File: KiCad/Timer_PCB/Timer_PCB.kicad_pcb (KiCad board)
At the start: 2 copper layers, 102 x 75.5 mm, 2 parts

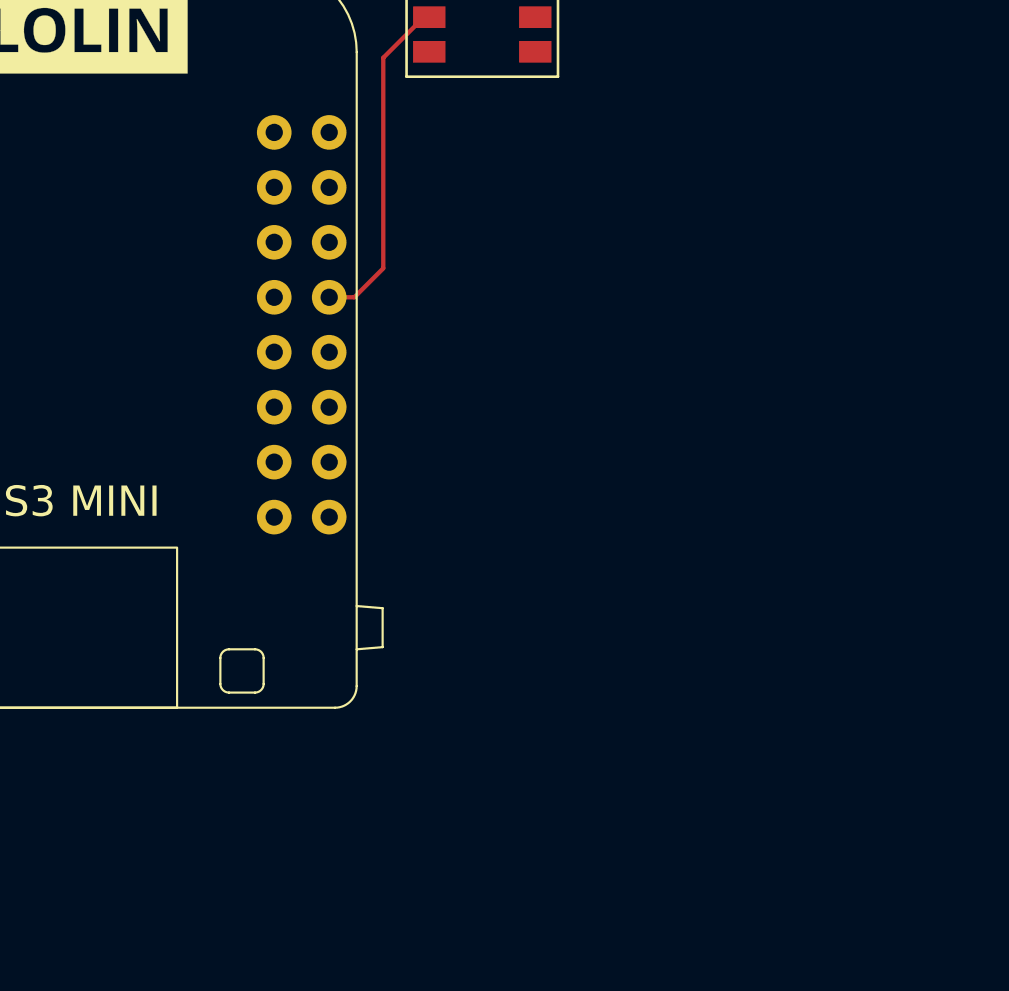
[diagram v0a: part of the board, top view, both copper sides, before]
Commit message: Ajout de la différenciation SMD et THT dans l'article composants electroniques. Ajout de la marche à suivre pour passer d'un composant physique à la réalisation de son schematic sur kicad. recherche de schéma du composant. recherche du numero de part sur JLC, recherche du package. modification du symbole pour y inclure ces information.
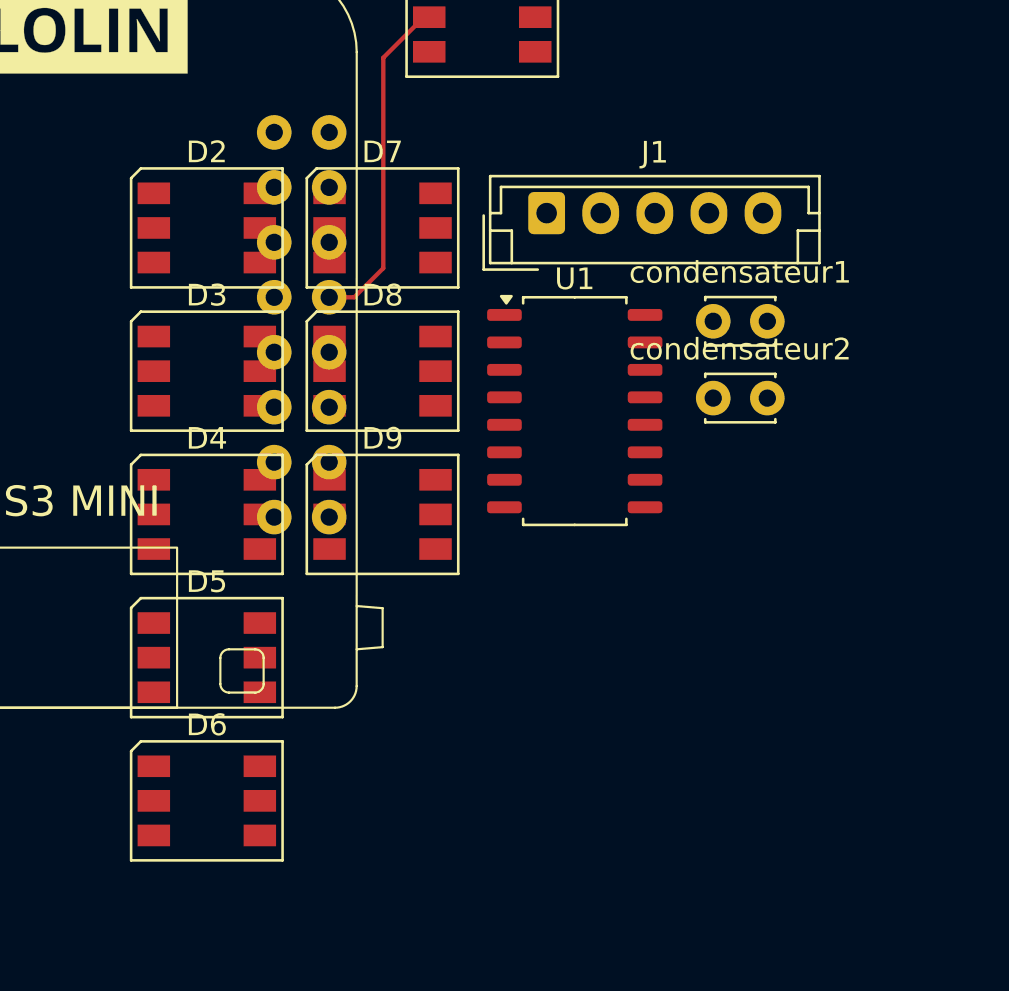
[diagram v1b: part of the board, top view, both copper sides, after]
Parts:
- added D2: WS2812, LED_SMD:LED_WS2812_PLCC6_5.0x5.0mm_P1.6mm, F.Cu at (101.3, 69.6)
- added D3: WS2812, LED_SMD:LED_WS2812_PLCC6_5.0x5.0mm_P1.6mm, F.Cu at (101.3, 76.3)
- added D4: WS2812, LED_SMD:LED_WS2812_PLCC6_5.0x5.0mm_P1.6mm, F.Cu at (101.3, 82.9)
- added D5: WS2812, LED_SMD:LED_WS2812_PLCC6_5.0x5.0mm_P1.6mm, F.Cu at (101.3, 89.5)
- added D6: WS2812, LED_SMD:LED_WS2812_PLCC6_5.0x5.0mm_P1.6mm, F.Cu at (101.3, 96.1)
- added D7: WS2812, LED_SMD:LED_WS2812_PLCC6_5.0x5.0mm_P1.6mm, F.Cu at (109.5, 69.6)
- added D8: WS2812, LED_SMD:LED_WS2812_PLCC6_5.0x5.0mm_P1.6mm, F.Cu at (109.5, 76.3)
- added D9: WS2812, LED_SMD:LED_WS2812_PLCC6_5.0x5.0mm_P1.6mm, F.Cu at (109.5, 82.9)
- added J1: JST_05, Connector_JST:JST_EH_B5B-EH-A_1x05_P2.50mm_Vertical, F.Cu at (117.0, 69.0)
- added U1: ULN2003, Package_SO:SOIC-16_4.55x10.3mm_P1.27mm, F.Cu at (118.3, 78.1)
- added condensateur1: 10uF, Capacitor_THT:C_Disc_D3.0mm_W2.0mm_P2.50mm, F.Cu at (124.8, 74.0)
- added condensateur2: 100nF, Capacitor_THT:C_Disc_D3.0mm_W2.0mm_P2.50mm, F.Cu at (124.8, 77.5)
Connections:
- D1 pad 1: unconnected-(D1-DOUT-Pad1) -> Net-(D1-DOUT)
- D1 pad 5: unconnected-(D1-VDD-Pad5) -> GND
- D1 pad 6: unconnected-(D1-VSS-Pad6) -> GND
- U2 pad 15: Net-(BT1-+) -> GND
- U2 pad 17: unconnected-(U2-GPIO33-Pad17) -> Net-(D1-DIN)
- U2 pad 2: unconnected-(U2-GPIO1-Pad2) -> M1A
- U2 pad 21: unconnected-(U2-GPIO38-Pad21) -> GND
- U2 pad 22: unconnected-(U2-GPIO36-Pad22) -> Net-(SW4-A)
- U2 pad 23: unconnected-(U2-GPIO34-Pad23) -> Net-(SW3-C)
- U2 pad 24: Net-(D1-DIN) -> Net-(SW3-A)
- U2 pad 25: unconnected-(U2-GPIO21-Pad25) -> GND
- U2 pad 26: unconnected-(U2-GPIO18-Pad26) -> GND
- U2 pad 27: unconnected-(U2-GPIO17-Pad27) -> GND
- U2 pad 28: unconnected-(U2-GPIO16-Pad28) -> Net-(SW1-A)
- U2 pad 29: Net-(BT1--) -> GND
- U2 pad 30: unconnected-(U2-GND-Pad30) -> GND
- U2 pad 5: unconnected-(U2-GPIO4-Pad5) -> M1B
- U2 pad 6: unconnected-(U2-GPIO5-Pad6) -> M1C
- U2 pad 7: unconnected-(U2-GPIO12-Pad7) -> M1D

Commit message: avancement de l'article sur l'utilisation de Kicad
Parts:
- added D10: WS2812, LED_SMD:LED_WS2812_PLCC6_5.0x5.0mm_P1.6mm, F.Cu at (105.2, 65.7)
- added D11: WS2812, LED_SMD:LED_WS2812_PLCC6_5.0x5.0mm_P1.6mm, F.Cu at (105.2, 72.3)
- added D12: WS2812, LED_SMD:LED_WS2812_PLCC6_5.0x5.0mm_P1.6mm, F.Cu at (105.2, 78.9)
- added D13: WS2812, LED_SMD:LED_WS2812_PLCC6_5.0x5.0mm_P1.6mm, F.Cu at (113.4, 65.7)
- added D14: WS2812, LED_SMD:LED_WS2812_PLCC6_5.0x5.0mm_P1.6mm, F.Cu at (113.4, 72.3)
- added D15: WS2812, LED_SMD:LED_WS2812_PLCC6_5.0x5.0mm_P1.6mm, F.Cu at (113.4, 78.9)
- added D16: WS2812, LED_SMD:LED_WS2812_PLCC6_5.0x5.0mm_P1.6mm, F.Cu at (121.5, 65.7)
- added D17: WS2812, LED_SMD:LED_WS2812_PLCC6_5.0x5.0mm_P1.6mm, F.Cu at (121.5, 72.3)
- added D18: WS2812, LED_SMD:LED_WS2812_PLCC6_5.0x5.0mm_P1.6mm, F.Cu at (121.5, 78.9)
- added J2: JST_05, Connector_JST:JST_EH_B5B-EH-A_1x05_P2.50mm_Vertical, F.Cu at (124.0, 84.8)
- added J3: JST_05, Connector_JST:JST_EH_B5B-EH-A_1x05_P2.50mm_Vertical, F.Cu at (124.0, 90.7)
- added U3: ULN2003, Package_SO:SOIC-16_4.55x10.3mm_P1.27mm, F.Cu at (106.0, 88.2)
- added U4: ULN2003, Package_SO:SOIC-16_4.55x10.3mm_P1.27mm, F.Cu at (115.7, 88.2)
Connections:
- net Net-(SW1-A) renamed Switch_Led_control_Down
- net Net-(SW3-A) renamed Switch_motor_2_Down
- net Net-(SW3-C) renamed Switch_motor_2_Up
- net Net-(SW4-A) renamed Switch_motor_3_Down
- U2 pad 10: unconnected-(U2-GPIO7-Pad10) -> M2C
- U2 pad 11: unconnected-(U2-GPIO11-Pad11) -> M2D
- U2 pad 12: unconnected-(U2-GPIO8-Pad12) -> M3A
- U2 pad 13: unconnected-(U2-GPIO10-Pad13) -> M3B
- U2 pad 14: unconnected-(U2-GPIO9-Pad14) -> M3C
- U2 pad 15: GND -> Net-(BT1-+)
- U2 pad 16: unconnected-(U2-GPIO14-Pad16) -> M3D
- U2 pad 17: Net-(D1-DIN) -> WS2812_Led
- U2 pad 21: GND -> Switch_motor_3_Up
- U2 pad 25: GND -> Switch_motor_1_Up
- U2 pad 26: GND -> Switch_motor_1_Down
- U2 pad 27: GND -> Switch_Led_control_Up
- U2 pad 29: GND -> unconnected-(U2-GND-Pad29)
- U2 pad 30: GND -> unconnected-(U2-GND-Pad30)
- U2 pad 31: unconnected-(U2-GPIO15-Pad31) -> Net-(U2-GPIO15)
- U2 pad 8: unconnected-(U2-GPIO6-Pad8) -> M2A
- U2 pad 9: unconnected-(U2-GPIO13-Pad9) -> M2B
- condensateur1 pad 1: GND -> Net-(U2-GPIO15)
- condensateur1 pad 2: GND -> Net-(BT1--)
- condensateur2 pad 1: GND -> Net-(U2-GPIO15)
- condensateur2 pad 2: GND -> Net-(BT1--)

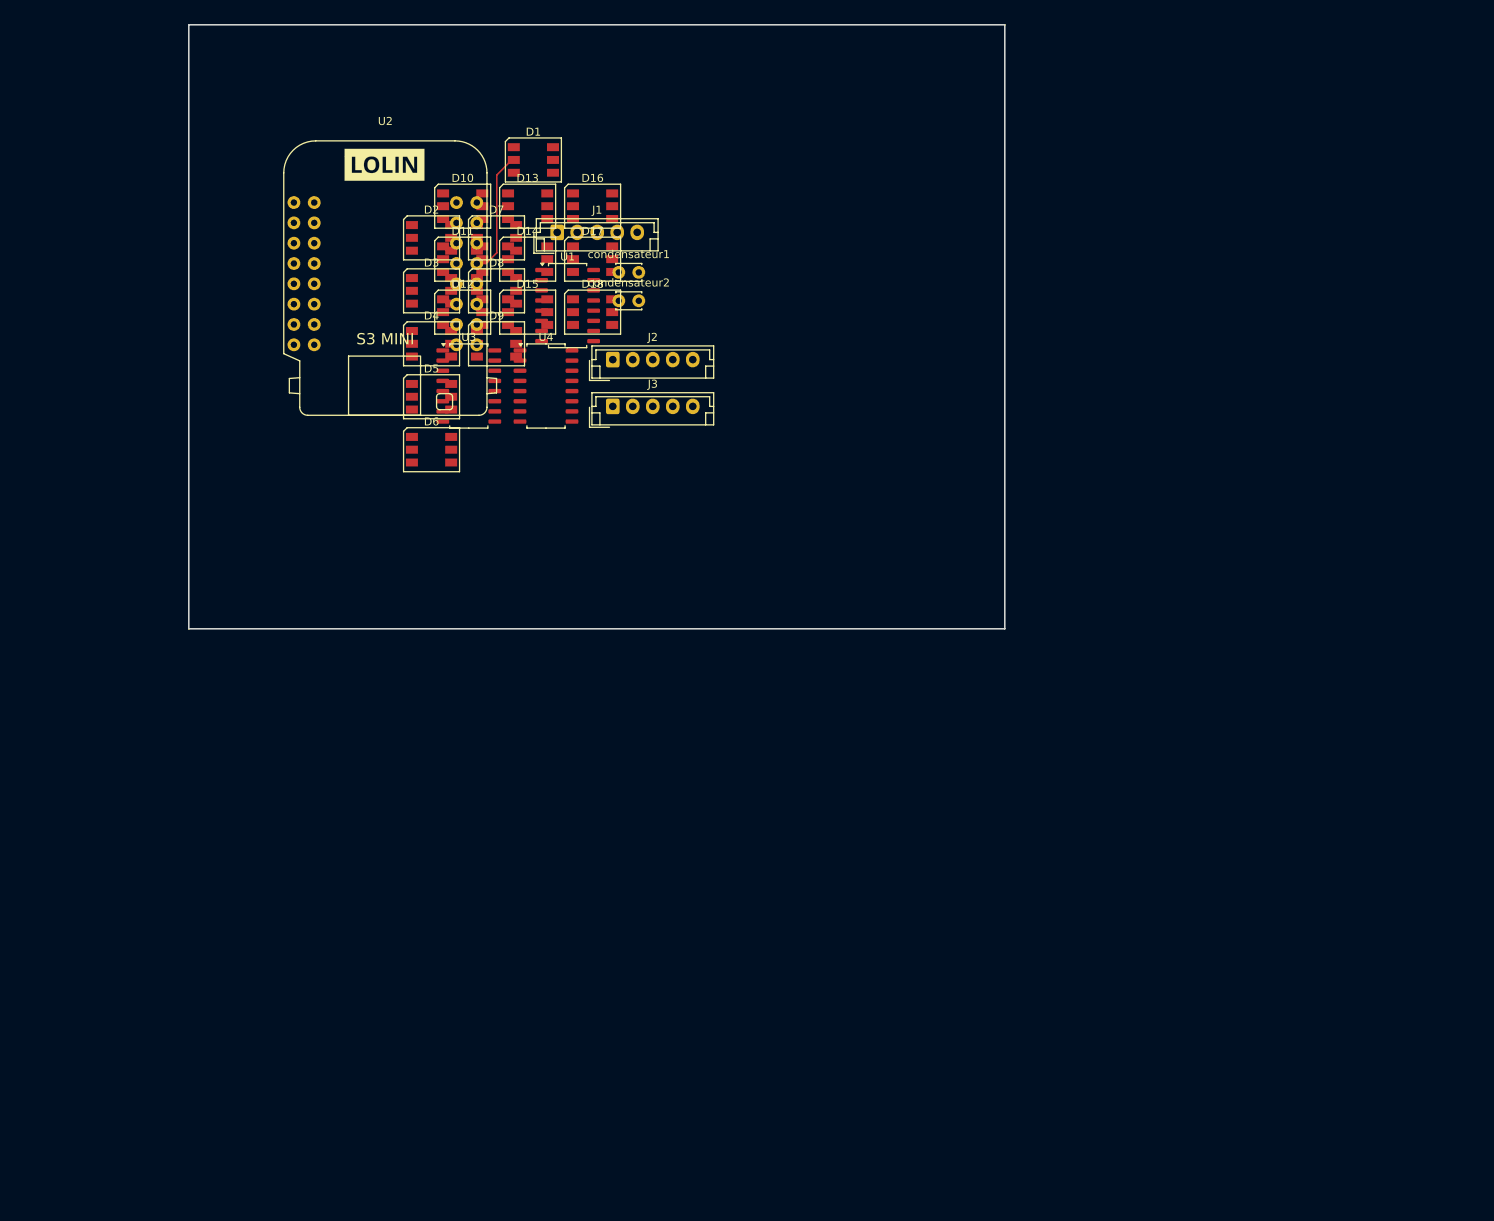
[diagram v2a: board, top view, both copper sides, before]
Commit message: dévellopement de l'article Kicad. Comment parametrer nbr couches PCB et créer zone connecté GND
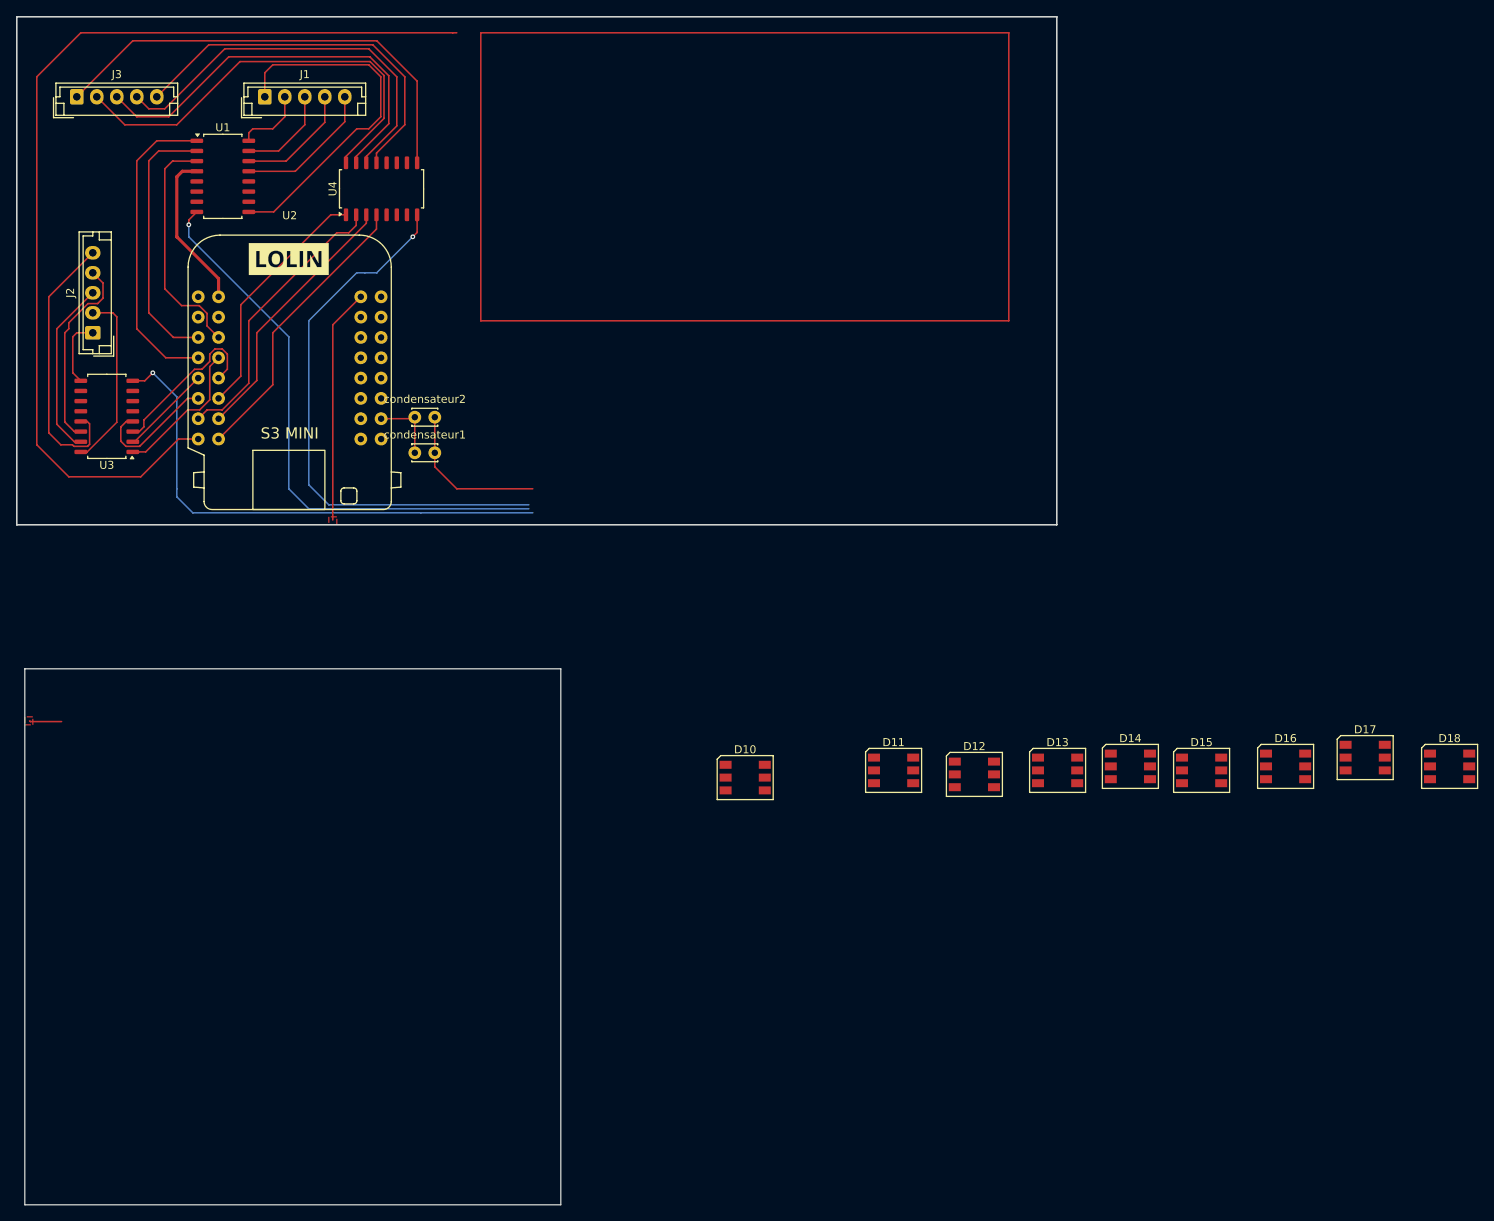
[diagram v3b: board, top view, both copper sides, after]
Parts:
- removed D1, D2, D3, D4, D5, D6, D7, D8, D9: WS2812, LED_SMD:LED_WS2812_PLCC6_5.0x5.0mm_P1.6mm
- moved D18 121.2 mm to (228.6, 135.7)
- moved D17 114.9 mm to (218.1, 134.6)
- moved D16 111.4 mm to (208.1, 135.7)
- moved D15 101.9 mm to (197.6, 136.2)
- moved D14 98.5 mm to (188.7, 135.7)
- moved D13 96.8 mm to (179.6, 136.2)
- moved D12 86.2 mm to (169.2, 136.7)
- moved D11 83.6 mm to (159.1, 136.2)
- moved D10 79.7 mm to (140.6, 137.1)
- moved J3 77.4 mm to (57.0, 52.0)
- moved J2 65.1 mm to (59.0, 81.5), turned to 90 degrees
- moved U1 46.0 mm to (75.2, 61.9)
- moved U3 45.4 mm to (60.8, 91.9), turned to 180 degrees
- moved J1 40.3 mm to (80.5, 52.0)
- moved condensateur1 34.0 mm to (99.2, 96.5)
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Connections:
- net WS2812_Led renamed WS2812_Med
- U2 pad 2: M1A -> M1D
- U2 pad 29: unconnected-(U2-GND-Pad29) -> GND
- U2 pad 30: unconnected-(U2-GND-Pad30) -> GND
- U2 pad 31: Net-(U2-GPIO15) -> unconnected-(U2-GPIO15-Pad31)
- U2 pad 7: M1D -> M1A
- condensateur1 pad 1: Net-(U2-GPIO15) -> GND
- condensateur2 pad 1: Net-(U2-GPIO15) -> GND
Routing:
- net GND: track 0.00 -> 214.3 mm, vias 0 -> 3
- net Net-(BT1-+): track 0.00 -> 124.6 mm
- net +5V: track 0.00 -> 111.3 mm
- net Net-(U4-O1): track 0.00 -> 54.2 mm
- net Net-(U4-O2): track 0.00 -> 51.7 mm
- net Net-(U4-O3): track 0.00 -> 50.0 mm
- net Net-(U4-O4): track 0.00 -> 47.6 mm
- net M1A: track 0.00 -> 38.7 mm
- net M3D: track 0.00 -> 36.2 mm
- net M3B: track 0.00 -> 35.7 mm
- net Net-(U3-O4): track 0.00 -> 34.5 mm
- net M3C: track 0.00 -> 33.1 mm
- net M1B: track 0.00 -> 33.0 mm
- net M3A: track 0.00 -> 30.7 mm
- net M1C: track 0.00 -> 29.6 mm
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- added copper zone on In2.Cu, net +5V
- added copper zone on In1.Cu, net GND
- added copper zone on F.Cu, net WS2812_Med
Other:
- board size 102 x 75.5 mm -> 130 x 148.5 mm
- copper layers 2 -> 4
